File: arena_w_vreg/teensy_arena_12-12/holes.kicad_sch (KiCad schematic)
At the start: 4 parts

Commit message: Wored on teensy arena.
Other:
- note added: "Notes 1. Should all the groung holes be 4.5mm (8-32??)"
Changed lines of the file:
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@@
     (stroke (width 0) (type default))
+  )
+  (text "Notes\n\n1. Should all the groung holes be 4.5mm (8-32??)\n"
+    (at 34.29 71.628 0)
+    (effects (font (size 2.54 2.54)) (justify left bottom))
   )
   (symbol (lib_id "power:GND") (at 68.58 35.179 0) (mirror y) (unit 1)

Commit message: Finished initial routing.
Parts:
- H1, H2, H3, H4: footprint MountingHole:MountingHole_3.2mm_M3_DIN965_Pad -> MountingHole:MountingHole_4.5mm_Pad
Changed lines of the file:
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@@
       (effects (font (size 1.27 1.27)) (justify left) hide)
     )
-    (property "Footprint" "MountingHole:MountingHole_3.2mm_M3_DIN965_Pad" (at 50.165 30.099 0)
+    (property "Footprint" "MountingHole:MountingHole_4.5mm_Pad" (at 50.165 30.099 0)
       (effects (font (size 1.27 1.27)) hide)
     )
@@
       (effects (font (size 1.27 1.27)) (justify left) hide)
     )
-    (property "Footprint" "MountingHole:MountingHole_3.2mm_M3_DIN965_Pad" (at 59.69 30.099 0)
+    (property "Footprint" "MountingHole:MountingHole_4.5mm_Pad" (at 59.69 30.099 0)
       (effects (font (size 1.27 1.27)) hide)
     )
@@
       (effects (font (size 1.27 1.27)) (justify left) hide)
     )
-    (property "Footprint" "MountingHole:MountingHole_3.2mm_M3_DIN965_Pad" (at 41.275 30.099 0)
+    (property "Footprint" "MountingHole:MountingHole_4.5mm_Pad" (at 41.275 30.099 0)
       (effects (font (size 1.27 1.27)) hide)
     )
@@
       (effects (font (size 1.27 1.27)) (justify left) hide)
     )
-    (property "Footprint" "MountingHole:MountingHole_3.2mm_M3_DIN965_Pad" (at 68.58 30.099 0)
+    (property "Footprint" "MountingHole:MountingHole_4.5mm_Pad" (at 68.58 30.099 0)
       (effects (font (size 1.27 1.27)) hide)
     )

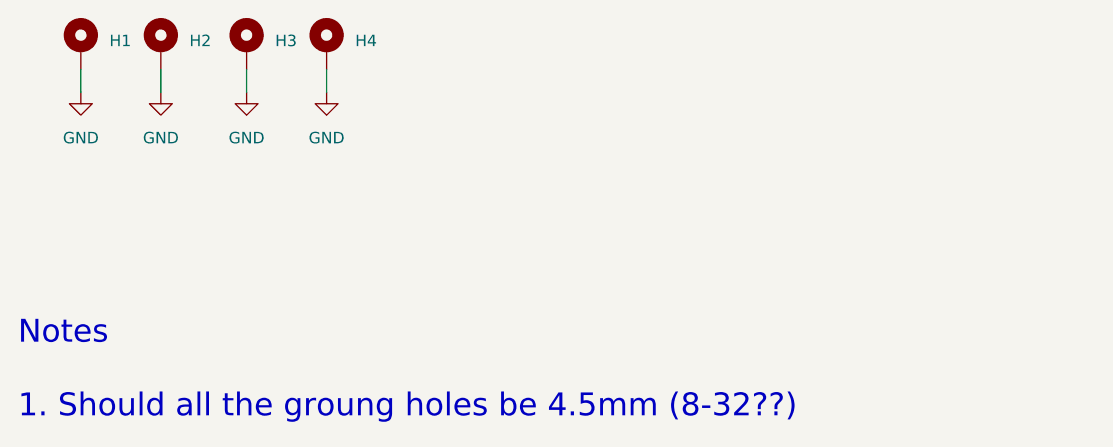
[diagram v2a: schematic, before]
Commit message: Removed old notes from schematic pdf.
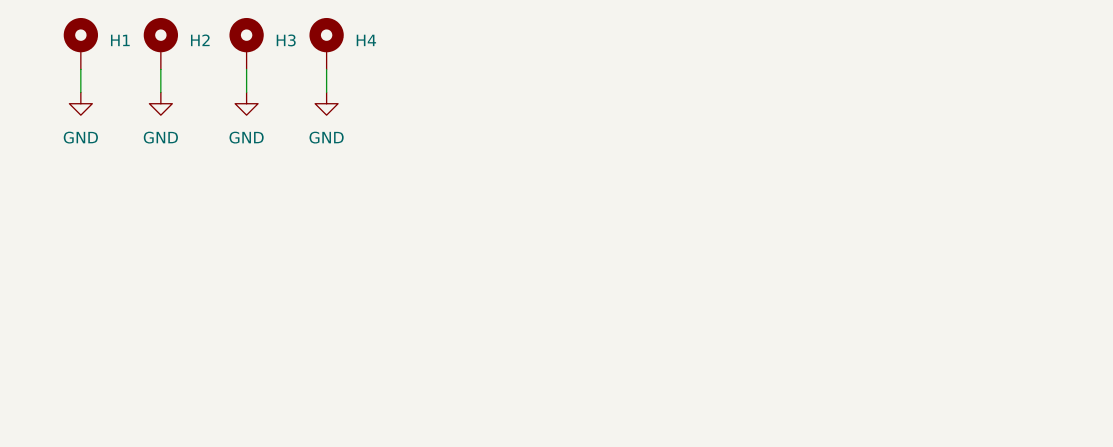
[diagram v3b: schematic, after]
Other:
- note removed: "Notes 1. Should all the groung holes be 4.5mm (8-32??)"
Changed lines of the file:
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@@
     (stroke (width 0) (type default))
-  )
-  (text "Notes\n\n1. Should all the groung holes be 4.5mm (8-32??)\n"
-    (at 34.29 71.628 0)
-    (effects (font (size 2.54 2.54)) (justify left bottom))
   )
   (symbol (lib_id "power:GND") (at 68.58 35.179 0) (mirror y) (unit 1)
